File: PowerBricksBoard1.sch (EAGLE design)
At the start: 11 parts

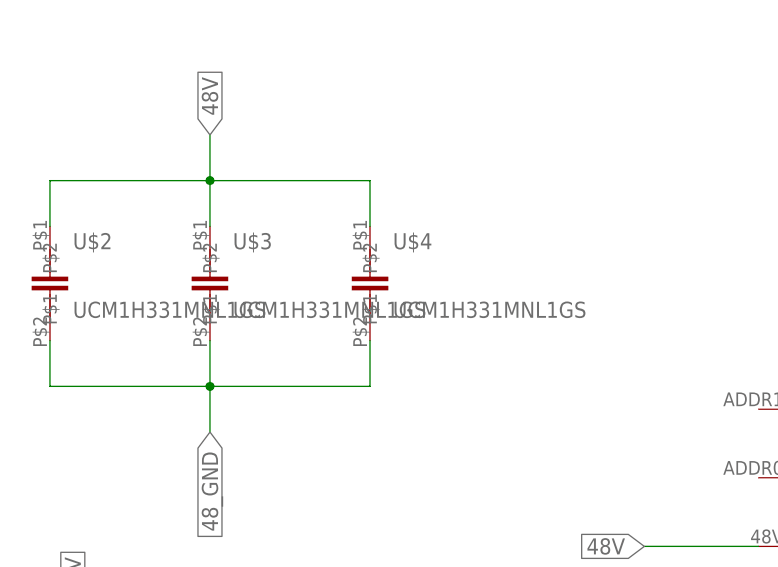
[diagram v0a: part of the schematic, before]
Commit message: Updated power bricks board with polarized capacitor schematic symbol
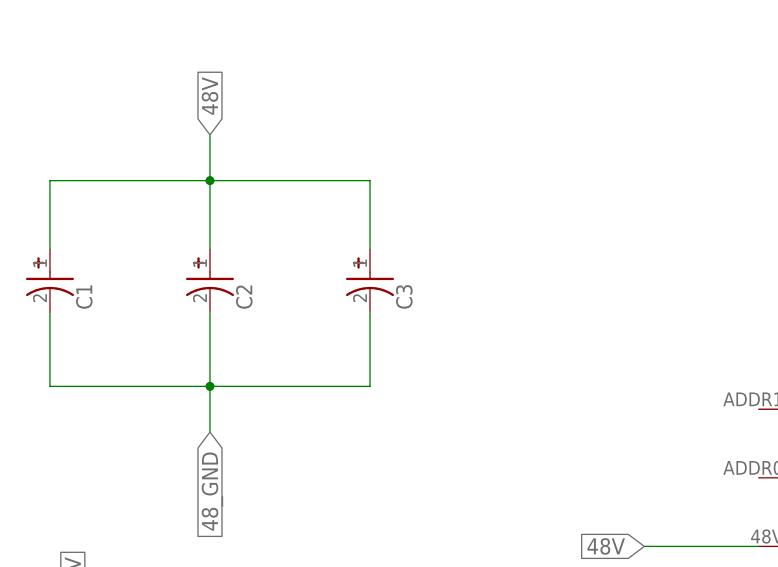
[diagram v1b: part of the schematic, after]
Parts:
- removed U$2, U$3, U$4: UCM1H331MNL1GS, UCM1H331MNL1GS:UCM1H331MNL1GS
- added C1, C2, C3: UCM1H331MNL1GS, UCM1H331MNL1GS:UCM1H331MNL1GS
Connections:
- net 48V: now also C1.+, C2.+, C3.+; no longer U$2.P$1, U$3.P$1, U$4.P$1
- net 48_GND: now also C1.-, C2.-, C3.-; no longer U$2.P$2, U$3.P$2, U$4.P$2
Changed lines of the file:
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@@
 <?xml version="1.0" encoding="utf-8"?>
 <!DOCTYPE eagle SYSTEM "eagle.dtd">
-<eagle version="9.5.0">
+<eagle version="9.6.2">
 <drawing>
 <settings>
@@
 <parts>
 <part name="FRAME1" library="frames" library_urn="urn:adsk.eagle:library:229" deviceset="A4L-LOC" device=""/>
-<part name="U$2" library="UCM1H331MNL1GS" deviceset="UCM1H331MNL1GS" device=""/>
-<part name="U$3" library="UCM1H331MNL1GS" deviceset="UCM1H331MNL1GS" device=""/>
-<part name="U$4" library="UCM1H331MNL1GS" deviceset="UCM1H331MNL1GS" device=""/>
 <part name="H1" library="SparkFun-Hardware" library_urn="urn:adsk.eagle:library:519" deviceset="STAND-OFF" device="" package3d_urn="urn:adsk.eagle:package:38630/1"/>
 <part name="H2" library="SparkFun-Hardware" library_urn="urn:adsk.eagle:library:519" deviceset="STAND-OFF" device="" package3d_urn="urn:adsk.eagle:package:38630/1"/>
@@
 <part name="D1" library="SparkFun-LED" library_urn="urn:adsk.eagle:library:529" deviceset="LED" device="0603" package3d_urn="urn:adsk.eagle:package:39354/1"/>
 <part name="R1" library="SparkFun-Resistors" library_urn="urn:adsk.eagle:library:532" deviceset="RESISTOR" device="0603" package3d_urn="urn:adsk.eagle:package:39650/1" value="470"/>
+<part name="C1" library="UCM1H331MNL1GS" deviceset="UCM1H331MNL1GS" device=""/>
+<part name="C2" library="UCM1H331MNL1GS" deviceset="UCM1H331MNL1GS" device=""/>
+<part name="C3" library="UCM1H331MNL1GS" deviceset="UCM1H331MNL1GS" device=""/>
 </parts>
 <sheets>
@@
 <attribute name="SHEET" x="100.965" y="-73.66" size="2.54" layer="94"/>
 </instance>
-<instance part="U$2" gate="G$1" x="-96.52" y="43.18" smashed="yes">
-<attribute name="NAME" x="-93.98" y="45.72" size="1.778" layer="95"/>
-<attribute name="VALUE" x="-93.98" y="38.1" size="1.778" layer="96"/>
-</instance>
-<instance part="U$3" gate="G$1" x="-78.74" y="43.18" smashed="yes">
-<attribute name="NAME" x="-76.2" y="45.72" size="1.778" layer="95"/>
-<attribute name="VALUE" x="-76.2" y="38.1" size="1.778" layer="96"/>
-</instance>
-<instance part="U$4" gate="G$1" x="-60.96" y="43.18" smashed="yes">
-<attribute name="NAME" x="-58.42" y="45.72" size="1.778" layer="95"/>
-<attribute name="VALUE" x="-58.42" y="38.1" size="1.778" layer="96"/>
-</instance>
 <instance part="H1" gate="G$1" x="109.22" y="15.24" smashed="yes"/>
 <instance part="H2" gate="G$1" x="104.14" y="15.24" smashed="yes"/>
@@
 <attribute name="VALUE" x="-92.456" y="-5.08" size="1.778" layer="96" font="vector" rot="R90" align="top-center"/>
 </instance>
+<instance part="C1" gate="G$1" x="-96.52" y="45.72" smashed="yes" rot="R270">
+<attribute name="NAME" x="-92.71" y="41.91" size="1.778" layer="95" rot="R270" align="center-left"/>
+</instance>
+<instance part="C2" gate="G$1" x="-78.74" y="45.72" smashed="yes" rot="R270">
+<attribute name="NAME" x="-74.93" y="41.91" size="1.778" layer="95" rot="R270" align="center-left"/>
+</instance>
+<instance part="C3" gate="G$1" x="-60.96" y="45.72" smashed="yes" rot="R270">
+<attribute name="NAME" x="-57.15" y="41.91" size="1.778" layer="95" rot="R270" align="center-left"/>
+</instance>
 </instances>
 <busses>
@@
 <net name="48V" class="0">
 <segment>
-<pinref part="U$2" gate="G$1" pin="P$1"/>
-<wire x1="-96.52" y1="48.26" x2="-96.52" y2="53.34" width="0.1524" layer="91"/>
+<wire x1="-96.52" y1="45.72" x2="-96.52" y2="53.34" width="0.1524" layer="91"/>
 <wire x1="-96.52" y1="53.34" x2="-78.74" y2="53.34" width="0.1524" layer="91"/>
-<pinref part="U$3" gate="G$1" pin="P$1"/>
-<wire x1="-78.74" y1="53.34" x2="-78.74" y2="48.26" width="0.1524" layer="91"/>
+<wire x1="-78.74" y1="53.34" x2="-78.74" y2="45.72" width="0.1524" layer="91"/>
 <wire x1="-78.74" y1="53.34" x2="-60.96" y2="53.34" width="0.1524" layer="91"/>
 <junction x="-78.74" y="53.34"/>
-<pinref part="U$4" gate="G$1" pin="P$1"/>
-<wire x1="-60.96" y1="53.34" x2="-60.96" y2="48.26" width="0.1524" layer="91"/>
+<wire x1="-60.96" y1="53.34" x2="-60.96" y2="45.72" width="0.1524" layer="91"/>
 <wire x1="-78.74" y1="53.34" x2="-78.74" y2="58.42" width="0.1524" layer="91"/>
 <label x="-78.74" y="58.42" size="1.778" layer="95" rot="R90" xref="yes"/>
+<pinref part="C1" gate="G$1" pin="+"/>
+<pinref part="C2" gate="G$1" pin="+"/>
+<pinref part="C3" gate="G$1" pin="+"/>
 </segment>
 <segment>
@@
 <net name="48_GND" class="0">
 <segment>
-<pinref part="U$4" gate="G$1" pin="P$2"/>
-<wire x1="-60.96" y1="35.56" x2="-60.96" y2="30.48" width="0.1524" layer="91"/>
+<wire x1="-60.96" y1="38.735" x2="-60.96" y2="30.48" width="0.1524" layer="91"/>
 <wire x1="-60.96" y1="30.48" x2="-78.74" y2="30.48" width="0.1524" layer="91"/>
-<pinref part="U$3" gate="G$1" pin="P$2"/>
-<wire x1="-78.74" y1="30.48" x2="-78.74" y2="35.56" width="0.1524" layer="91"/>
+<wire x1="-78.74" y1="30.48" x2="-78.74" y2="38.735" width="0.1524" layer="91"/>
 <wire x1="-78.74" y1="30.48" x2="-96.52" y2="30.48" width="0.1524" layer="91"/>
 <junction x="-78.74" y="30.48"/>
-<pinref part="U$2" gate="G$1" pin="P$2"/>
-<wire x1="-96.52" y1="30.48" x2="-96.52" y2="35.56" width="0.1524" layer="91"/>
+<wire x1="-96.52" y1="30.48" x2="-96.52" y2="38.735" width="0.1524" layer="91"/>
 <wire x1="-78.74" y1="30.48" x2="-78.74" y2="25.4" width="0.1524" layer="91"/>
 <label x="-78.74" y="25.4" size="1.778" layer="95" rot="R270" xref="yes"/>
-</segment>
-<segment>
+<pinref part="C3" gate="G$1" pin="-"/>
+<pinref part="C2" gate="G$1" pin="-"/>
+<pinref part="C1" gate="G$1" pin="-"/>
+</segment>
+<segment>

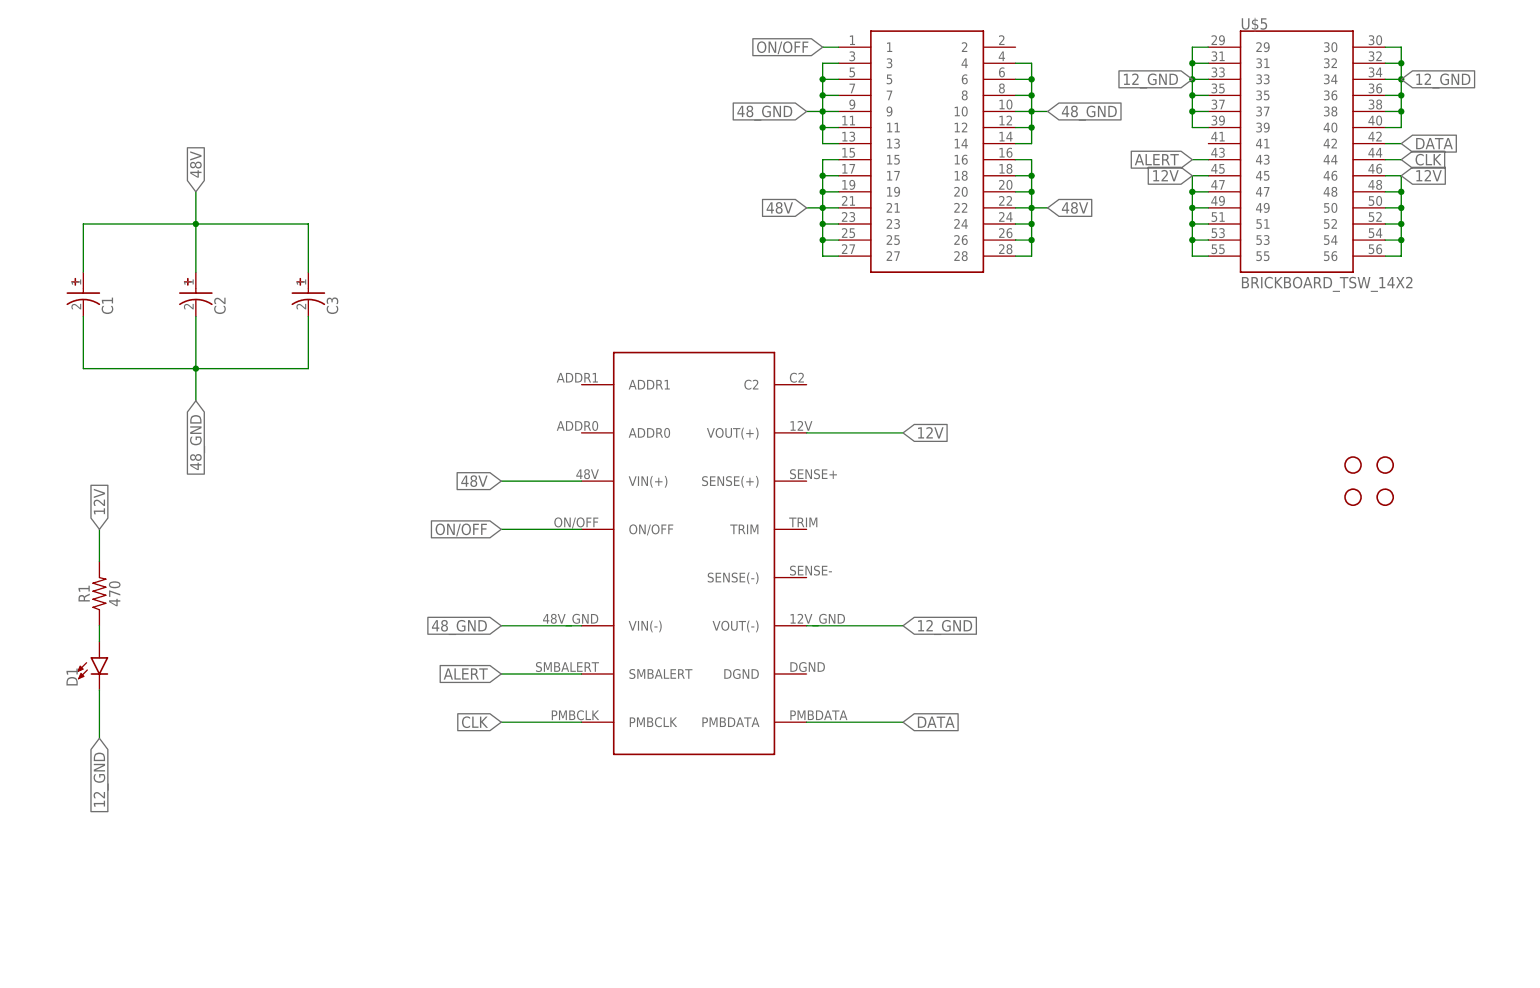
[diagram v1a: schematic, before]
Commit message: Updated board w/ latest x12 update, otherwise same as before
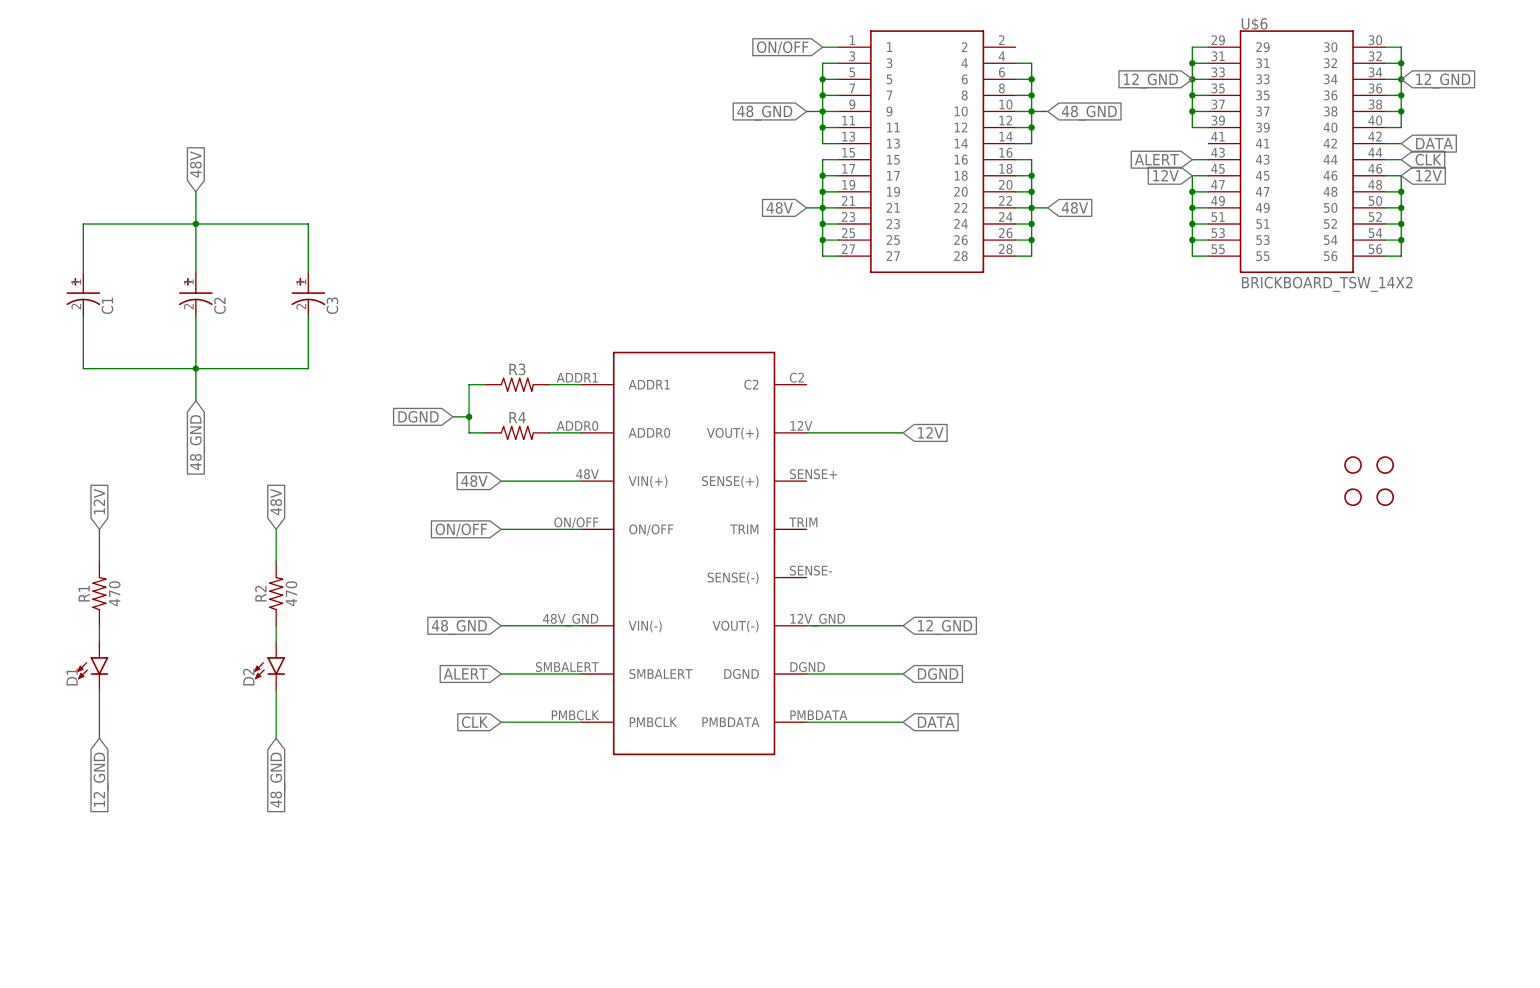
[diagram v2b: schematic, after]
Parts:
- removed U$5: BRICKBOARD_TSW_14X2, Dist_to_Brickboard_Connector:BRICKBOARD_TSW_14X2
- added D2: (no value), SparkFun-LED:LED0603
- added R2: 470, SparkFun-Resistors:RESISTOR0603
- added R3, R4: (no value), SparkFun-Resistors:RESISTOR0603
- added U$6: BRICKBOARD_TSW_14X2, Dist_to_Brickboard_Connector_brick:BRICKBOARD_TSW_14X2
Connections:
- new net DGND: R3.1, R4.1, U$1.DGND
- new net N$2: D2.A, R2.1
- new net N$3: R3.2, U$1.ADDR1
- new net N$4: R4.2, U$1.ADDR0
- net 12V: now also U$6.45, U$6.46, U$6.47, U$6.48, U$6.49, U$6.50, U$6.51, U$6.52, U$6.53, U$6.54, U$6.55, U$6.56; no longer U$5.45, U$5.46, U$5.47, U$5.48, U$5.49, U$5.50, U$5.51, U$5.52, U$5.53, U$5.54, U$5.55, U$5.56
- net 12_GND: now also U$6.29, U$6.30, U$6.31, U$6.32, U$6.33, U$6.34, U$6.35, U$6.36, U$6.37, U$6.38, U$6.39, U$6.40; no longer U$5.29, U$5.30, U$5.31, U$5.32, U$5.33, U$5.34, U$5.35, U$5.36, U$5.37, U$5.38, U$5.39, U$5.40
- net 48V: now also R2.2, U$6.15, U$6.16, U$6.17, U$6.18, U$6.19, U$6.20, U$6.21, U$6.22, U$6.23, U$6.24, U$6.25, U$6.26, U$6.27, U$6.28; no longer U$5.15, U$5.16, U$5.17, U$5.18, U$5.19, U$5.20, U$5.21, U$5.22, U$5.23, U$5.24, U$5.25, U$5.26, U$5.27, U$5.28
- net 48_GND: now also D2.C, U$6.10, U$6.11, U$6.12, U$6.13, U$6.14, U$6.3, U$6.4, U$6.5, U$6.6, U$6.7, U$6.8, U$6.9; no longer U$5.10, U$5.11, U$5.12, U$5.13, U$5.14, U$5.3, U$5.4, U$5.5, U$5.6, U$5.7, U$5.8, U$5.9
- net ALERT: now also U$6.43; no longer U$5.43
- net CLK: now also U$6.44; no longer U$5.44
- net DATA: now also U$6.42; no longer U$5.42
- net ON/OFF: now also U$6.1; no longer U$5.1

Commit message: nya
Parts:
- removed R3: (no value), SparkFun-Resistors:RESISTOR0603
- added U$2: PMBUSTABLE, PMBUS Resistors:PMBUSTABLE
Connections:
- net DGND: now also U$2.1; no longer R3.1
- net N$3: now also U$2.2; no longer R3.2
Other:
- moved on the sheet: R4
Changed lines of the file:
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@@
 <layer number="115" name="ReferenceISLANDS" color="7" fill="1" visible="yes" active="yes"/>
 <layer number="116" name="Patch_BOT" color="9" fill="4" visible="yes" active="yes"/>
+<layer number="117" name="PM_Ref" color="7" fill="1" visible="no" active="no"/>
 <layer number="118" name="Rect_Pads" color="7" fill="1" visible="yes" active="yes"/>
+<layer number="119" name="PF_Ref" color="7" fill="1" visible="no" active="no"/>
+<layer number="120" name="WFL_Ref" color="7" fill="1" visible="no" active="no"/>
 <layer number="121" name="_tsilk" color="7" fill="1" visible="yes" active="yes"/>
 <layer number="122" name="_bsilk" color="7" fill="1" visible="yes" active="yes"/>
@@
 <part name="R2" library="SparkFun-Resistors" library_urn="urn:adsk.eagle:library:532" deviceset="RESISTOR" device="0603" package3d_urn="urn:adsk.eagle:package:39650/1" value="470"/>
 <part name="U$6" library="Dist_to_Brickboard_Connector_brick" deviceset="BRICKBOARD_TSW_14X2" device="" package3d_urn="urn:adsk.eagle:package:23225958/2"/>
-<part name="R3" library="SparkFun-Resistors" library_urn="urn:adsk.eagle:library:532" deviceset="RESISTOR" device="0603" package3d_urn="urn:adsk.eagle:package:39650/1" value=" "/>
-<part name="R4" library="SparkFun-Resistors" library_urn="urn:adsk.eagle:library:532" deviceset="RESISTOR" device="0603" package3d_urn="urn:adsk.eagle:package:39650/1" value=" "/>
 <part name="C1" library="UCM1H331MNL1GS" deviceset="UCM1H331MNL1GS" device=""/>
 <part name="C2" library="UCM1H331MNL1GS" deviceset="UCM1H331MNL1GS" device=""/>
 <part name="C3" library="UCM1H331MNL1GS" deviceset="UCM1H331MNL1GS" device=""/>
+<part name="R4" library="SparkFun-Resistors" library_urn="urn:adsk.eagle:library:532" deviceset="RESISTOR" device="0603" package3d_urn="urn:adsk.eagle:package:39650/1" value=" "/>
+<part name="U$2" library="PMBUS Resistors" deviceset="PMBUSTABLE" device=""/>
 </parts>
 <sheets>
@@
 <attribute name="VALUE" x="86.36" y="43.18" size="1.778" layer="95"/>
 </instance>
-<instance part="R3" gate="G$1" x="-27.94" y="27.94" smashed="yes">
-<attribute name="NAME" x="-27.94" y="29.464" size="1.778" layer="95" font="vector" align="bottom-center"/>
-<attribute name="VALUE" x="-27.94" y="26.416" size="1.778" layer="96" font="vector" align="top-center"/>
-</instance>
-<instance part="R4" gate="G$1" x="-27.94" y="20.32" smashed="yes">
-<attribute name="NAME" x="-27.94" y="21.844" size="1.778" layer="95" font="vector" align="bottom-center"/>
-<attribute name="VALUE" x="-27.94" y="18.796" size="1.778" layer="96" font="vector" align="top-center"/>
-</instance>
 <instance part="C1" gate="G$1" x="-96.52" y="45.72" smashed="yes" rot="R270">
 <attribute name="NAME" x="-92.71" y="41.91" size="1.778" layer="95" rot="R270" align="center-left"/>
@@
 <instance part="C3" gate="G$1" x="-60.96" y="45.72" smashed="yes" rot="R270">
 <attribute name="NAME" x="-57.15" y="41.91" size="1.778" layer="95" rot="R270" align="center-left"/>
+</instance>
+<instance part="R4" gate="G$1" x="-33.02" y="20.32" smashed="yes">
+<attribute name="NAME" x="-33.02" y="21.844" size="1.778" layer="95" font="vector" align="bottom-center"/>
+<attribute name="VALUE" x="-33.02" y="18.796" size="1.778" layer="96" font="vector" align="top-center"/>
+</instance>
+<instance part="U$2" gate="G$1" x="-33.02" y="27.94" smashed="yes">
+<attribute name="NAME" x="-33.02" y="29.464" size="1.778" layer="95" font="vector" align="bottom-center"/>
 </instance>
 </instances>
@@
 </segment>
 <segment>
-<pinref part="R3" gate="G$1" pin="1"/>
-<wire x1="-33.02" y1="27.94" x2="-35.56" y2="27.94" width="0.1524" layer="91"/>
+<wire x1="-38.1" y1="20.32" x2="-45.72" y2="20.32" width="0.1524" layer="91"/>
+<wire x1="-45.72" y1="27.94" x2="-45.72" y2="22.86" width="0.1524" layer="91"/>
+<wire x1="-45.72" y1="22.86" x2="-45.72" y2="20.32" width="0.1524" layer="91"/>
+<wire x1="-45.72" y1="22.86" x2="-48.26" y2="22.86" width="0.1524" layer="91"/>
+<junction x="-45.72" y="22.86"/>
+<label x="-48.26" y="22.86" size="1.778" layer="95" rot="R180" xref="yes"/>
 <pinref part="R4" gate="G$1" pin="1"/>
-<wire x1="-33.02" y1="20.32" x2="-35.56" y2="20.32" width="0.1524" layer="91"/>
-<wire x1="-35.56" y1="27.94" x2="-35.56" y2="22.86" width="0.1524" layer="91"/>
-<wire x1="-35.56" y1="22.86" x2="-35.56" y2="20.32" width="0.1524" layer="91"/>
-<wire x1="-35.56" y1="22.86" x2="-38.1" y2="22.86" width="0.1524" layer="91"/>
-<junction x="-35.56" y="22.86"/>
-<label x="-38.1" y="22.86" size="1.778" layer="95" rot="R180" xref="yes"/>
+<wire x1="-45.72" y1="27.94" x2="-38.1" y2="27.94" width="0.1524" layer="91"/>
+<pinref part="U$2" gate="G$1" pin="1"/>
 </segment>
 </net>
@@
 <segment>
 <pinref part="U$1" gate="G$1" pin="ADDR1"/>
-<pinref part="R3" gate="G$1" pin="2"/>
-<wire x1="-17.78" y1="27.94" x2="-22.86" y2="27.94" width="0.1524" layer="91"/>
+<wire x1="-27.94" y1="27.94" x2="-17.78" y2="27.94" width="0.1524" layer="91"/>
+<pinref part="U$2" gate="G$1" pin="2"/>
 </segment>
 </net>
 <net name="N$4" class="0">
 <segment>
+<pinref part="R4" gate="G$1" pin="2"/>
 <pinref part="U$1" gate="G$1" pin="ADDR0"/>
-<pinref part="R4" gate="G$1" pin="2"/>
-<wire x1="-17.78" y1="20.32" x2="-22.86" y2="20.32" width="0.1524" layer="91"/>
+<wire x1="-27.94" y1="20.32" x2="-17.78" y2="20.32" width="0.1524" layer="91"/>
 </segment>
 </net>
@@
 </drawing>
 <compatibility>
+<note version="6.3" minversion="6.2.2" severity="warning">
+Since Version 6.2.2 text objects can contain more than one line,
+which will not be processed correctly with this version.
+</note>
 <note version="8.2" severity="warning">
 Since Version 8.2, EAGLE supports online libraries. The ids
